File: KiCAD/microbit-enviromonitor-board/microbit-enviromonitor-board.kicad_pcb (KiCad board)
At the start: 2 copper layers, 45.7 x 62.2 mm, 8 parts, among them J1 12V, J2 SERIAL, J3 3V3, J4 PUMP, Q1 TIP41C, U1 REGULATOR

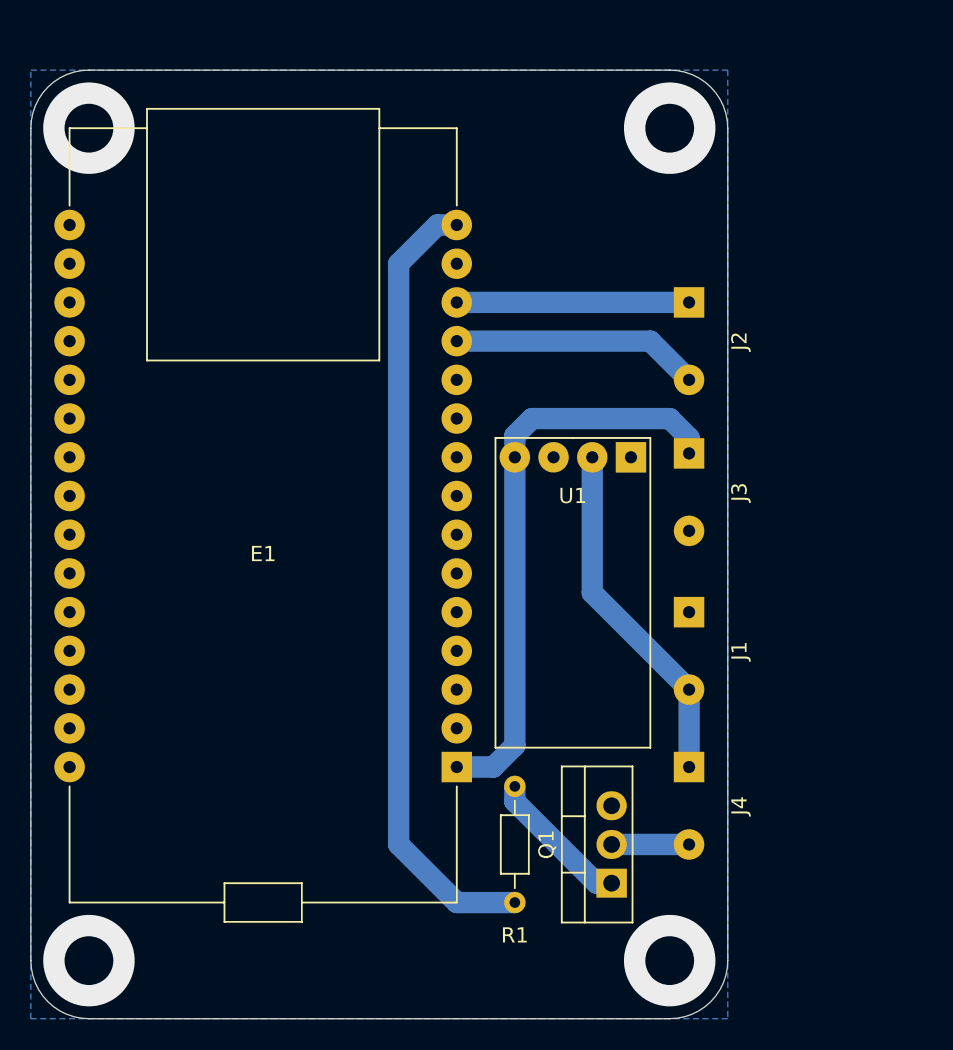
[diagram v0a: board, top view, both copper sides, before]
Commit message: Updated serial port
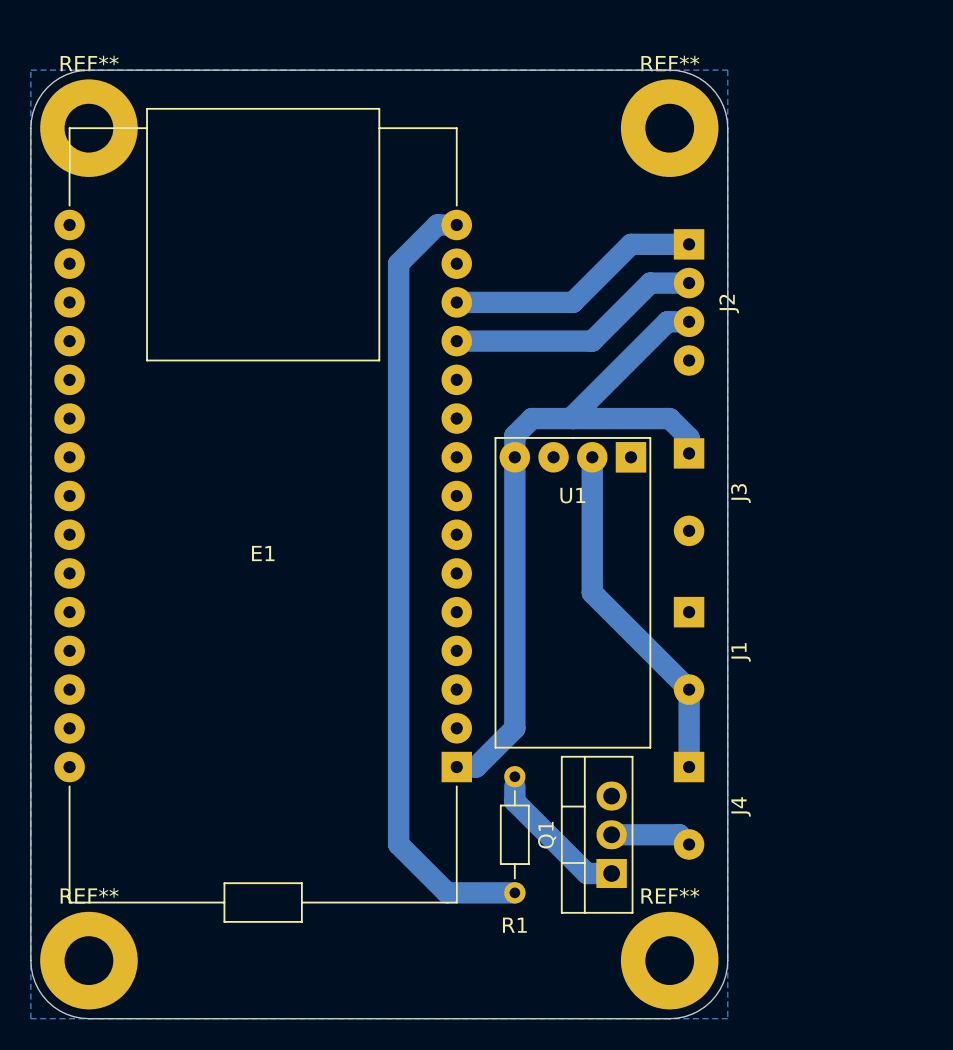
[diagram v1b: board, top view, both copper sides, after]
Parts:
- added REF**: MountingHole_3.2mm_M3_Pad, MountingHole:MountingHole_3.2mm_M3_Pad, F.Cu at (3.81, 58.4)
- added REF**: MountingHole_3.2mm_M3_Pad, MountingHole:MountingHole_3.2mm_M3_Pad, F.Cu at (41.9, 58.4)
- added REF**: MountingHole_3.2mm_M3_Pad, MountingHole:MountingHole_3.2mm_M3_Pad, F.Cu at (41.9, 3.81)
- added REF**: MountingHole_3.2mm_M3_Pad, MountingHole:MountingHole_3.2mm_M3_Pad, F.Cu at (3.81, 3.81)
- J2: footprint headers:2_double_spaced -> headers:4x1
- moved J2 2.54 mm to (43.2, 15.2)
- moved Q1 0.64 mm to (38.1, 52.7)
- moved R1 0.64 mm to (31.8, 46.4)
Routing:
- net +3V3: track 38.2 -> 47.8 mm
- net Net-(E1-Pad13): track 15.2 -> 16.8 mm
- net Net-(E1-Pad12): track 16.3 -> 16.8 mm
- net (no net): vias 4 -> 0

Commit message: Board changes
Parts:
- removed the REF** at (3.81, 58.4)
- removed the REF** at (41.9, 58.4)
- removed the REF** at (41.9, 3.81)
- added REF**: MountingHole_3.2mm_M3_Pad, MountingHole:MountingHole_3.2mm_M3_Pad, F.Cu at (3.81, 41.9)
- added REF**: MountingHole_3.2mm_M3_Pad, MountingHole:MountingHole_3.2mm_M3_Pad, F.Cu at (54.6, 41.9)
- added REF**: MountingHole_3.2mm_M3_Pad, MountingHole:MountingHole_3.2mm_M3_Pad, F.Cu at (54.6, 3.81)
- J1, J3, J4: footprint headers:2_double_spaced -> headers:screw_terminal
- moved J1 19.1 mm to (54.6, 22.9)
- moved J4 19.0 mm to (54.6, 33.0)
- moved J3 18.8 mm to (54.6, 12.7)
- moved U1 15.5 mm to (44.5, 12.7)
- moved Q1 15.0 mm to (47.0, 40.6)
- moved R1 15.0 mm to (40.6, 34.3)
- moved J2 10.2 mm to (44.5, 5.08), turned to 0 degrees
- moved E1 8.13 mm to (21.6, 24.1)
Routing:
- net Net-(E1-Pad13): track 16.8 -> 9.34 mm
- net +3V3: track 47.8 -> 52.4 mm
- net Net-(E1-Pad12): track 16.8 -> 12.6 mm
- net Net-(J4-Pad2): track 5.34 -> 8.67 mm
- net +12V: track 23.0 -> 21.5 mm
- net /PUMP: track 51.9 -> 50.4 mm
- net Net-(Q1-Pad1): track 9.30 -> 10.0 mm
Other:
- board size 45.7 x 62.2 mm -> 58.4 x 45.7 mm
- board text added: "MICROBIT ENVIROBOARD V1"

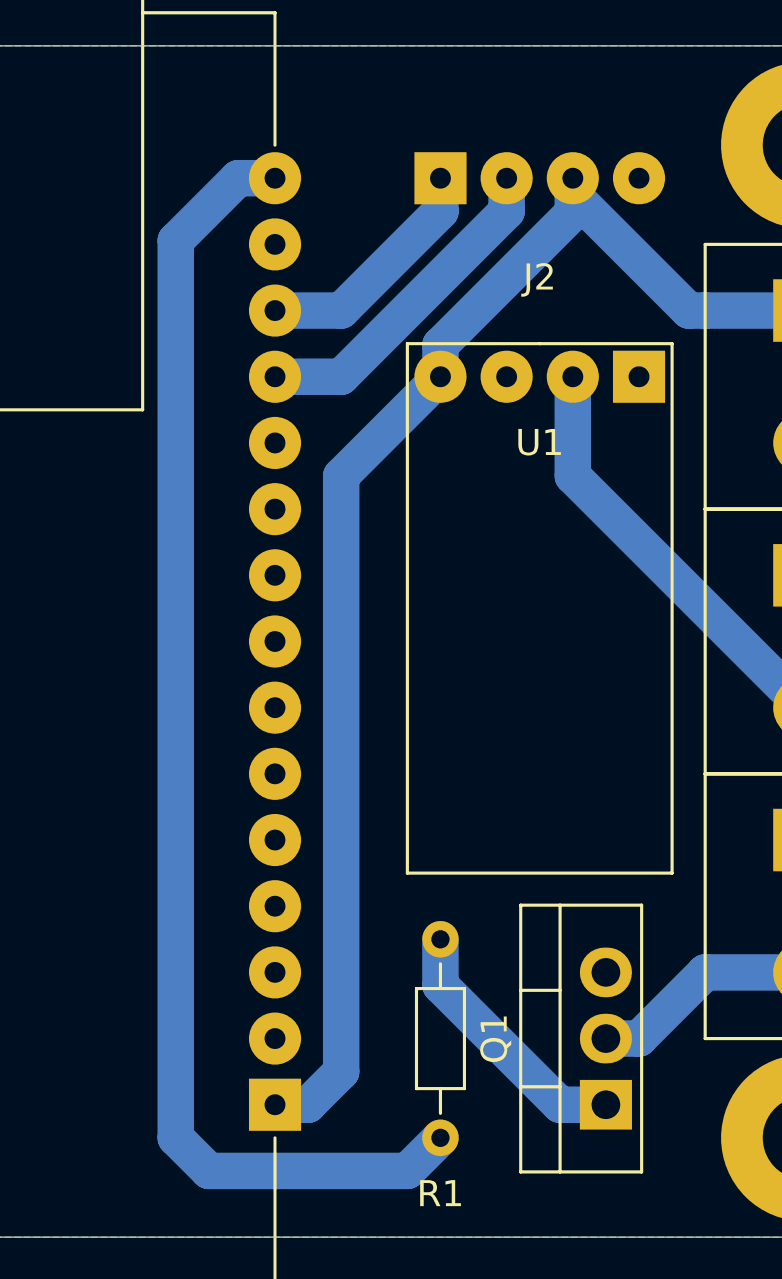
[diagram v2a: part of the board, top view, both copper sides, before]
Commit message: Added pump switch
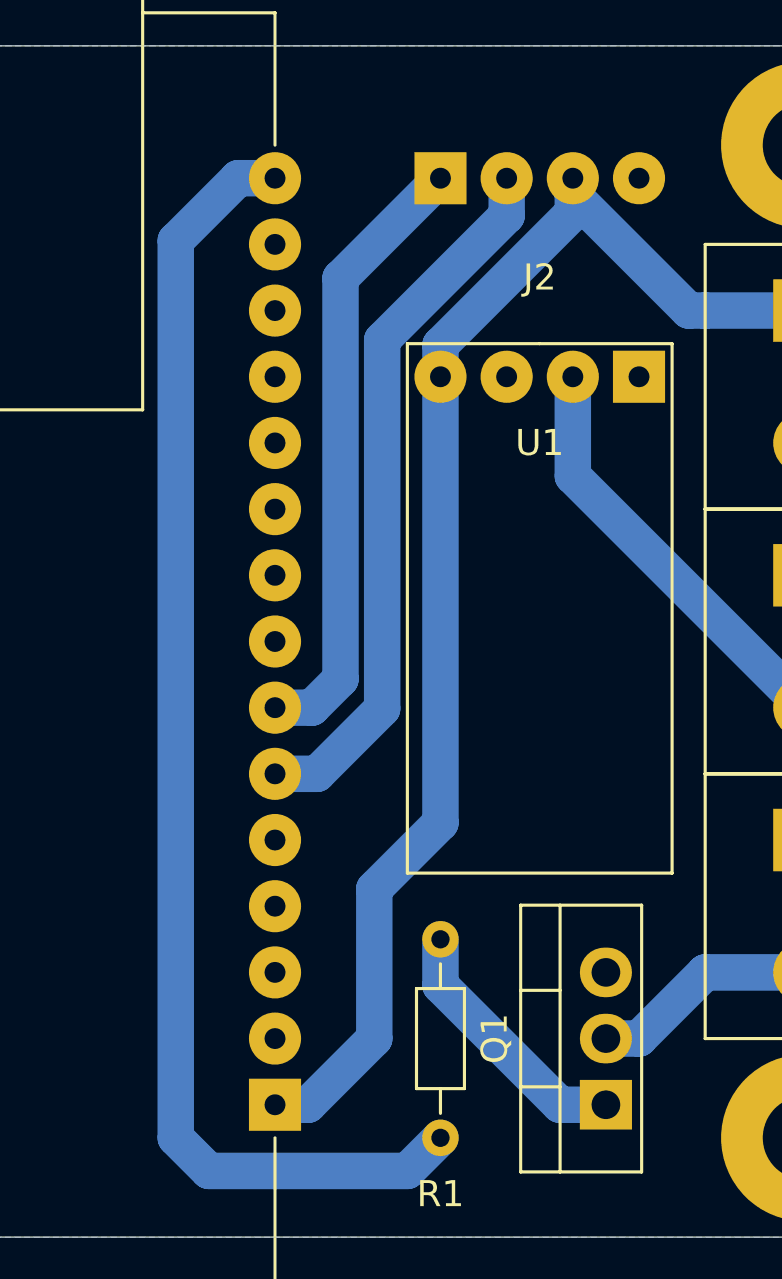
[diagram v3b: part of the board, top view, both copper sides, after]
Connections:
- J2 pad 1: Net-(E1-Pad13) -> Net-(E1-Pad7)
- J2 pad 2: Net-(E1-Pad12) -> Net-(E1-Pad6)
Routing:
- net Net-(E1-Pad6): track 0.00 -> 27.5 mm
- net Net-(E1-Pad7): track 0.00 -> 23.8 mm
- net Net-(E1-Pad12): track 12.6 -> 0.00 mm
- net Net-(E1-Pad13): track 9.34 -> 0.00 mm
